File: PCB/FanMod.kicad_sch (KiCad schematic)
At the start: 5 parts, among them J6 FAN1, Q5 IRLML0030

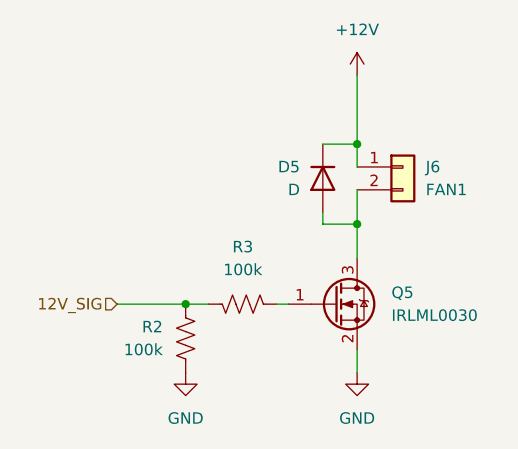
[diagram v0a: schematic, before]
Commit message: Updated footprints/layout for better connections.
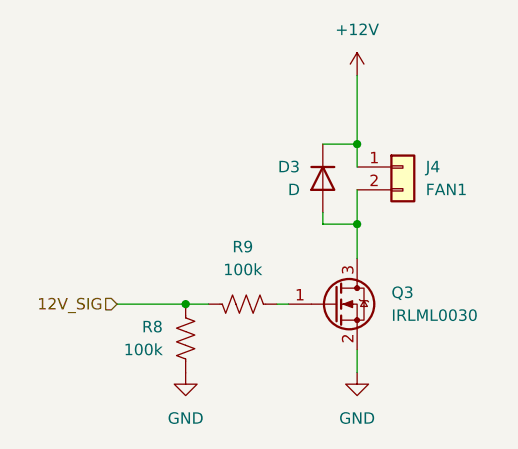
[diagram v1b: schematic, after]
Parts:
- D3: renamed from D5; footprint LED_SMD:LED_0805_2012Metric -> Diode_SMD:D_0805_2012Metric
- renumbered J6 to J4, Q5 to Q3, R2 to R8, R3 to R9
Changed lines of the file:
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@@
 		(dnp no)
 		(fields_autoplaced yes)
-		(property "Reference" "#PWR012"
+		(property "Reference" "#PWR018"
 			(at 143.51 91.44 0)
 			(effects
@@
 				(path "/1aabcb47-8889-428a-a945-776d6a97cab7/421cca7f-fdb9-4201-aba1-be75cef2f951"
 					(reference "#PWR018")
+					(unit 1)
+				)
+				(path "/1aabcb47-8889-428a-a945-776d6a97cab7/577f8a55-9002-4f4f-a791-a795000d5de3"
+					(reference "#PWR0101")
 					(unit 1)
 				)
@@
 		(on_board yes)
 		(dnp no)
-		(property "Reference" "D5"
+		(property "Reference" "D3"
 			(at 137.16 62.2299 90)
 			(effects
@@
 			)
 		)
-		(property "Footprint" "LED_SMD:LED_0805_2012Metric"
+		(property "Footprint" "Diode_SMD:D_0805_2012Metric"
 			(at 139.7 63.5 0)
 			(effects
@@
 		(dnp no)
 		(fields_autoplaced yes)
-		(property "Reference" "R3"
+		(property "Reference" "R9"
 			(at 130.81 71.12 90)
 			(effects
@@
 		(dnp no)
 		(fields_autoplaced yes)
-		(property "Reference" "#PWR020"
+		(property "Reference" "#PWR017"
 			(at 143.51 55.88 0)
 			(effects
@@
 		(dnp no)
 		(fields_autoplaced yes)
-		(property "Reference" "#PWR019"
+		(property "Reference" "#PWR016"
 			(at 124.46 91.44 0)
 			(effects
@@
 		(on_board yes)
 		(dnp no)
-		(property "Reference" "R2"
+		(property "Reference" "R8"
 			(at 121.92 80.0099 0)
 			(effects
@@
 		(dnp no)
 		(fields_autoplaced yes)
-		(property "Reference" "J6"
+		(property "Reference" "J4"
 			(at 151.13 62.2299 0)
 			(effects
@@
 		(dnp no)
 		(fields_autoplaced yes)
-		(property "Reference" "Q5"
+		(property "Reference" "Q3"
 			(at 147.32 76.1999 0)
 			(effects
